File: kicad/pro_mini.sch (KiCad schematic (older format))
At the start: 11 parts, among them IC1 ATMEGA328P-A, P1 FTDI, P2 DIGITAL, P3 CONN_01X12

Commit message: Layout
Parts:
- added C5, C6: 1uF, Capacitors_SMD:C_0805_HandSoldering, symbol C
- added U1: MCP1700T-3302E, TO_SOT_Packages_SMD:SOT89-3_Housing_Handsoldering, symbol MCP1700T-3302E
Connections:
- net A4: now also P2.11 (P11); no longer P2.12 (P12)
- net A5: now also P2.12 (P12); no longer P2.11 (P11)
- net GND: now also C5.2, C6.2, U1.1 (GND)
- net VCC: now also C6.1, U1.3 (VOUT)
- net RAW: now reaches P3.12 (P12)
- net RAW: now also C5.1, U1.2 (VIN)
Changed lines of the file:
@@
 LIBS:contrib
 LIBS:valves
+LIBS:pro_mini
+LIBS:pro_mini-cache
 EELAYER 25 0
 EELAYER END
@@
 Text GLabel 3800 3800 2    60   Input ~ 0
 A7
+Text GLabel 3800 3700 2    60   Input ~ 0
+A4
 Text GLabel 3800 3600 2    60   Input ~ 0
-A4
-Text GLabel 3800 3700 2    60   Input ~ 0
 A5
 $Comp
@@
 Text Label 9800 3200 2    60   ~ 0
 RESET
+$Comp
+L MCP1700T-3302E U1
+U 1 1 573733AD
+P 2500 1850
+F 0 "U1" H 2300 2050 50  0000 C CNN
+F 1 "MCP1700T-3302E" H 2500 2050 50  0000 L CNN
+F 2 "TO_SOT_Packages_SMD:SOT89-3_Housing_Handsoldering" H 2500 1950 50  0000 C CIN
+F 3 "" H 2500 1850 50  0000 C CNN
+	1    2500 1850
+	1    0    0    -1
+$EndComp
+$Comp
+L C C6
+U 1 1 573737E7
+P 3100 1950
+F 0 "C6" H 3125 2050 50  0000 L CNN
+F 1 "1uF" H 3125 1850 50  0000 L CNN
+F 2 "Capacitors_SMD:C_0805_HandSoldering" H 3138 1800 50  0001 C CNN
+F 3 "" H 3100 1950 50  0000 C CNN
+	1    3100 1950
+	1    0    0    -1
+$EndComp
+$Comp
+L C C5
+U 1 1 57373849
+P 1850 1950
+F 0 "C5" H 1875 2050 50  0000 L CNN
+F 1 "1uF" H 1875 1850 50  0000 L CNN
+F 2 "Capacitors_SMD:C_0805_HandSoldering" H 1888 1800 50  0001 C CNN
+F 3 "" H 1850 1950 50  0000 C CNN
+	1    1850 1950
+	1    0    0    -1
+$EndComp
+$Comp
+L GND #PWR08
+U 1 1 5737390F
+P 2500 2300
+F 0 "#PWR08" H 2500 2050 50  0001 C CNN
+F 1 "GND" H 2500 2150 50  0000 C CNN
+F 2 "" H 2500 2300 50  0000 C CNN
+F 3 "" H 2500 2300 50  0000 C CNN
+	1    2500 2300
+	1    0    0    -1
+$EndComp
+Wire Wire Line
+	1500 1800 2100 1800
+Wire Wire Line
+	2900 1800 3700 1800
+Wire Wire Line
+	1850 2100 3100 2100
+Connection ~ 2500 2100
+Wire Wire Line
+	2500 2300 2500 2100
+Text GLabel 1500 1800 0    60   Input ~ 0
+RAW
+Connection ~ 1850 1800
+Text GLabel 3700 1800 2    60   Input ~ 0
+VCC
+Connection ~ 3100 1800
+Text GLabel 4800 3600 0    60   Input ~ 0
+RAW
 $EndSCHEMATC

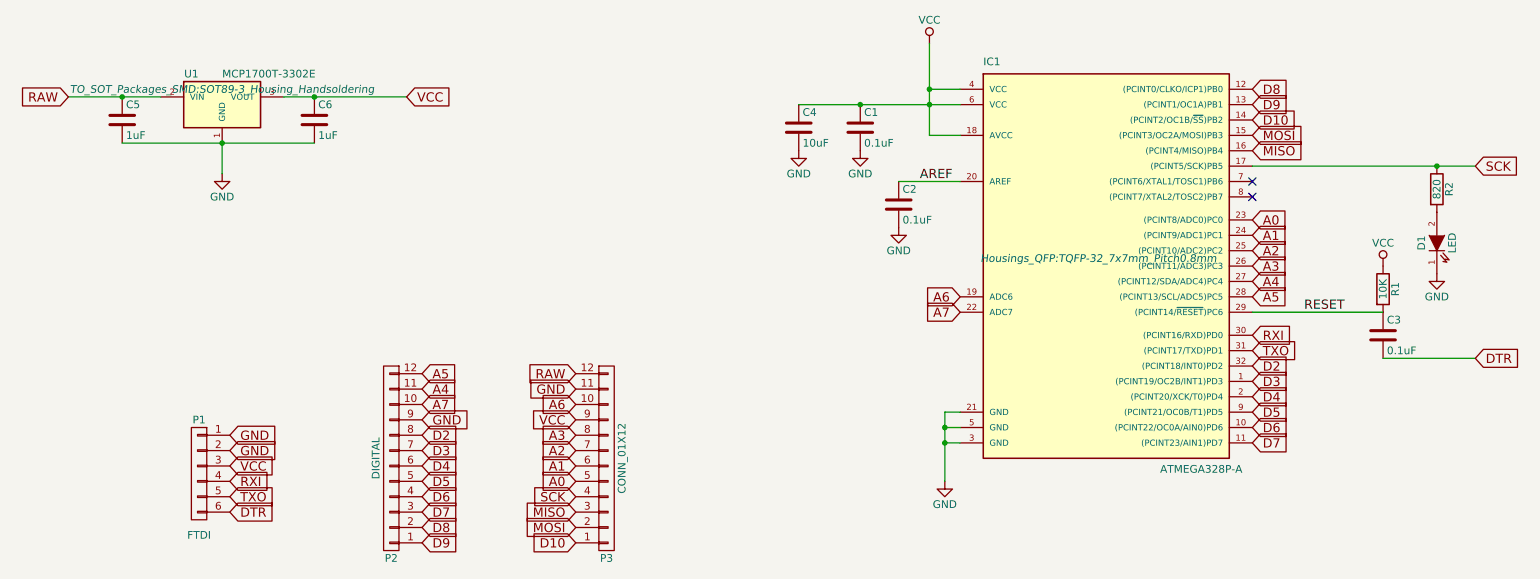
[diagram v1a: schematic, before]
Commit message: Optional external oscillator & reset restored to side header
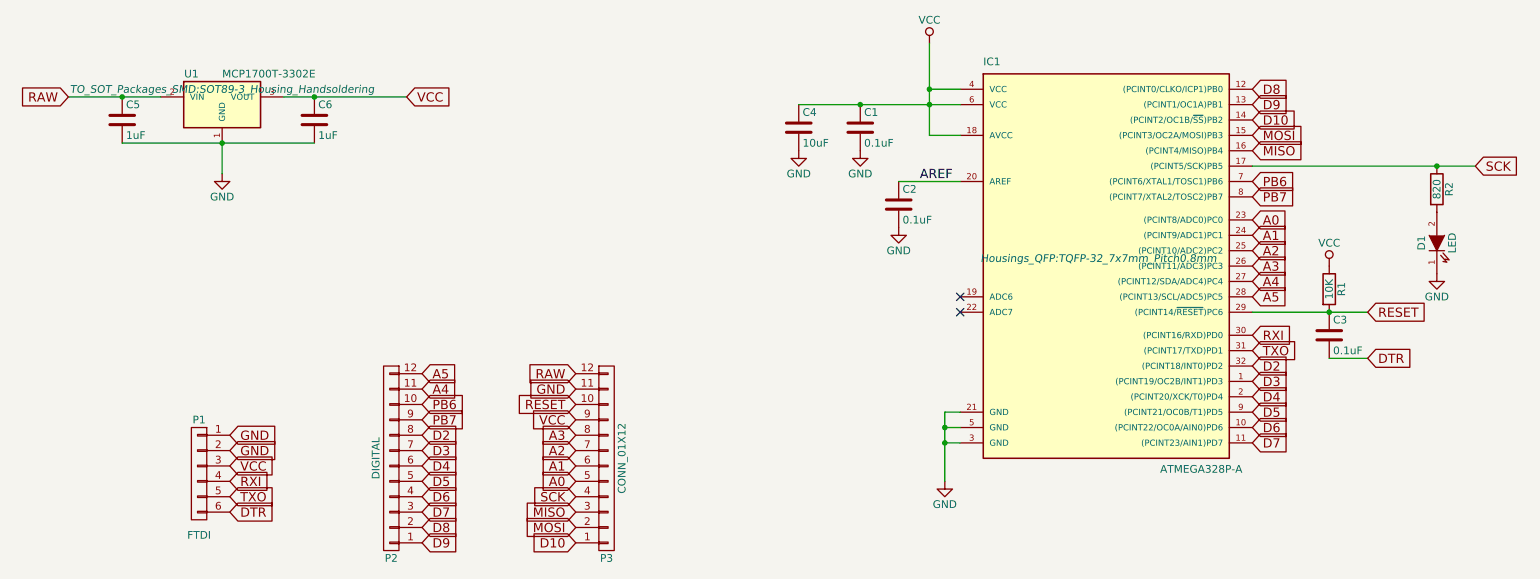
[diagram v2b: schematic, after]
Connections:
- net GND: no longer P2.9 (P9)
- net RESET: now also P3.10 (P10)
- net PB6: now reaches IC1.7 ((PCINT6/XTAL1/TOSC1)PB6)
- net PB6: now also P2.10 (P10)
- net PB7: now reaches IC1.8 ((PCINT7/XTAL2/TOSC2)PB7)
- net PB7: now also P2.9 (P9)
- net A6: no longer names the net of IC1.19 (ADC6)
- net A6: no longer P3.10 (P10)
- net A7: no longer names the net of IC1.22 (ADC7)
- net A7: no longer P2.10 (P10)
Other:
- moved on the sheet: C3, R1
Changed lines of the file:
@@
 Text GLabel 10650 2250 2    60   Input ~ 0
 SCK
-NoConn ~ 9200 2350
-NoConn ~ 9200 2450
 Text GLabel 9200 2600 2    60   Input ~ 0
 A0
@@
 L R R1
 U 1 1 5736F4EB
-P 10050 3050
-F 0 "R1" V 10130 3050 50  0000 C CNN
-F 1 "10K" V 10050 3050 50  0000 C CNN
-F 2 "Resistors_SMD:R_0805_HandSoldering" V 9980 3050 50  0001 C CNN
-F 3 "" H 10050 3050 50  0000 C CNN
-	1    10050 3050
+P 9700 3050
+F 0 "R1" V 9780 3050 50  0000 C CNN
+F 1 "10K" V 9700 3050 50  0000 C CNN
+F 2 "Resistors_SMD:R_0805_HandSoldering" V 9630 3050 50  0001 C CNN
+F 3 "" H 9700 3050 50  0000 C CNN
+	1    9700 3050
 	1    0    0    -1
 $EndComp
@@
 L VCC #PWR06
 U 1 1 5736F56F
-P 10050 2900
-F 0 "#PWR06" H 10050 2750 50  0001 C CNN
-F 1 "VCC" H 10050 3050 50  0000 C CNN
-F 2 "" H 10050 2900 50  0000 C CNN
-F 3 "" H 10050 2900 50  0000 C CNN
-	1    10050 2900
+P 9700 2900
+F 0 "#PWR06" H 9700 2750 50  0001 C CNN
+F 1 "VCC" H 9700 3050 50  0000 C CNN
+F 2 "" H 9700 2900 50  0000 C CNN
+F 3 "" H 9700 2900 50  0000 C CNN
+	1    9700 2900
 	1    0    0    -1
 $EndComp
@@
 L C C3
 U 1 1 5736F5A2
-P 10050 3350
-F 0 "C3" H 10075 3450 50  0000 L CNN
-F 1 "0.1uF" H 10075 3250 50  0000 L CNN
-F 2 "Capacitors_SMD:C_0805_HandSoldering" H 10088 3200 50  0001 C CNN
-F 3 "" H 10050 3350 50  0000 C CNN
-	1    10050 3350
-	1    0    0    -1
-$EndComp
-Wire Wire Line
-	9200 3200 10050 3200
-Text GLabel 10650 3500 2    60   Input ~ 0
+P 9700 3350
+F 0 "C3" H 9725 3450 50  0000 L CNN
+F 1 "0.1uF" H 9725 3250 50  0000 L CNN
+F 2 "Capacitors_SMD:C_0805_HandSoldering" H 9738 3200 50  0001 C CNN
+F 3 "" H 9700 3350 50  0000 C CNN
+	1    9700 3350
+	1    0    0    -1
+$EndComp
+Text GLabel 9950 3500 2    60   Input ~ 0
 DTR
 Wire Wire Line
-	10650 3500 10050 3500
+	9950 3500 9700 3500
 $Comp
 L CONN_01X06 P1
@@
 	-1   0    0    1
 $EndComp
-Text GLabel 3800 3900 2    60   Input ~ 0
-GND
 Text GLabel 3800 4000 2    60   Input ~ 0
 D2
@@
 Text GLabel 4800 4700 0    60   Input ~ 0
 D10
-Text GLabel 7300 3100 0    60   Input ~ 0
-A6
-Text GLabel 7300 3200 0    60   Input ~ 0
-A7
-Text GLabel 4800 3800 0    60   Input ~ 0
-A6
-Text GLabel 3800 3800 2    60   Input ~ 0
-A7
 Text GLabel 3800 3700 2    60   Input ~ 0
 A4
@@
 $EndComp
 Connection ~ 6650 1850
-Text Label 9800 3200 2    60   ~ 0
-RESET
 $Comp
 L MCP1700T-3302E U1
@@
 Text GLabel 4800 3600 0    60   Input ~ 0
 RAW
+NoConn ~ 7300 3200
+Text GLabel 9200 2350 2    60   Input ~ 0
+PB6
+Text GLabel 9200 2450 2    60   Input ~ 0
+PB7
+Text GLabel 3800 3800 2    60   Input ~ 0
+PB6
+Text GLabel 3800 3900 2    60   Input ~ 0
+PB7
+NoConn ~ 7300 3100
+Text GLabel 9950 3200 2    60   Input ~ 0
+RESET
+Text GLabel 4800 3800 0    60   Input ~ 0
+RESET
+Wire Wire Line
+	9200 3200 9950 3200
+Connection ~ 9700 3200
 $EndSCHEMATC
